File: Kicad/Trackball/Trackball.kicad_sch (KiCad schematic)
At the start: 52 parts, among them J1 Battery, J10 Conn_01x04_Female, J11 Conn_01x04_Female, J12 Conn_01x04_Female, J13 Conn_01x04_Female, J14 Conn_01x04_Female, J15 Conn_01x04_Female, J17 Conn_01x04_Female, J18 Conn_01x03_Pin, J19 Conn_01x03_Pin, J2 Conn_01x04_Male, J20 Conn_01x03_Socket, J21 Conn_01x03_Socket, J3 Conn_01x04_Male, J4 Conn_01x04_Male, J5 Conn_01x04_Male, J7 Conn_01x04_Male, J8 Conn_01x04_Male, J9 Conn_01x04_Male, SW1 SW_SPDT, SW2 SW_SPDT, SW3 SW_SPDT, U1 ProMicro, U3 TCR2EF19, U4 PMW3610

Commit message: B4: Base,  Cover, 52.5 mm ball platform ready. TODO: add 44mm platform.
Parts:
- removed H2: MountingHole_Pad, MountingHole:MountingHole_2.5mm_Pad, symbol Mechanical:MountingHole_Pad
- removed J11, J14, J17: Conn_01x04_Female, Connector_PinSocket_2.54mm:PinSocket_1x04_P2.54mm_Vertical, symbol Connector:Conn_01x04_Female
- removed J7, J8, J9: Conn_01x04_Male, Connector_PinHeader_2.54mm:PinHeader_1x04_P2.54mm_Vertical, symbol Connector:Conn_01x04_Male
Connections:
- net GND_T is gone; now on net GNDA: H3.1, H6.1, H7.1
- net Button1: now also J12.4 (Pin_4); no longer MX1.1 (COL)
- net Button2: now also MX2.2 (ROW); no longer J2.2 (Pin_2)
- net Button3: now also MX3.2 (ROW); no longer J2.3 (Pin_3)
- net Button4: now also J15.4 (Pin_4); no longer MX4.2 (ROW)
- net Button5: now also MX5.1 (COL); no longer J3.2 (Pin_2)
- net Button6: now also MX6.1 (COL); no longer J3.3 (Pin_3)
- net GND: now also J10.1 (Pin_1), J10.2 (Pin_2), J10.3 (Pin_3), J10.4 (Pin_4), J12.1 (Pin_1), J12.2 (Pin_2), J12.3 (Pin_3), J13.1 (Pin_1), J13.2 (Pin_2), J13.3 (Pin_3), J13.4 (Pin_4), J15.1 (Pin_1), J15.2 (Pin_2), J15.3 (Pin_3), MX2.1 (COL), MX3.1 (COL), MX5.2 (ROW), MX6.2 (ROW); no longer H4.1, H5.1, J4.1 (Pin_1), J4.2 (Pin_2), J4.3 (Pin_3), J4.4 (Pin_4), J5.1 (Pin_1), J5.2 (Pin_2), J5.3 (Pin_3), J5.4 (Pin_4), MX1.2 (ROW), MX4.1 (COL)
- net GNDA: now also H4.1, H5.1, J2.1 (Pin_1), J2.2 (Pin_2), J2.3 (Pin_3), J2.4 (Pin_4), J3.1 (Pin_1), J3.2 (Pin_2), J3.3 (Pin_3), J3.4 (Pin_4), J4.1 (Pin_1), J4.2 (Pin_2), J4.3 (Pin_3), MX1.2 (ROW), MX4.1 (COL); no longer J12.1 (Pin_1), J12.2 (Pin_2), J12.3 (Pin_3), J12.4 (Pin_4), J15.1 (Pin_1), J15.2 (Pin_2), J15.3 (Pin_3), J15.4 (Pin_4), MX2.1 (COL), MX3.1 (COL), MX5.2 (ROW), MX6.2 (ROW)
- new net: J4.4 (Pin_4), MX1.1 (COL)
- new net: J5.4 (Pin_4), MX4.2 (ROW)
- new net: J5.1 (Pin_1), J5.2 (Pin_2), J5.3 (Pin_3)
- no-connect marks 11 -> 2
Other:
- note removed: "Top PCB Support."
- moved on the sheet: J10, J12, J13, J15, J2, J3, J4, J5, MX1, MX4

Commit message: B4: Trying to hoax JLC to think the bottom plate is small - added pad holes instead of simple holes.
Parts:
- added H10, H11, H12, H13, H14, H15, H16, H2, H8, H9: MountingHole_Pad, MountingHole:MountingHole_3.7mm_Pad, symbol Mechanical:MountingHole_Pad
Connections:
- net GND: now also H12.1, H13.1, H14.1, H15.1, H16.1
- new net GNDB: H10.1, H11.1, H2.1, H8.1, H9.1
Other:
- note added: "Cover Plate Holes"

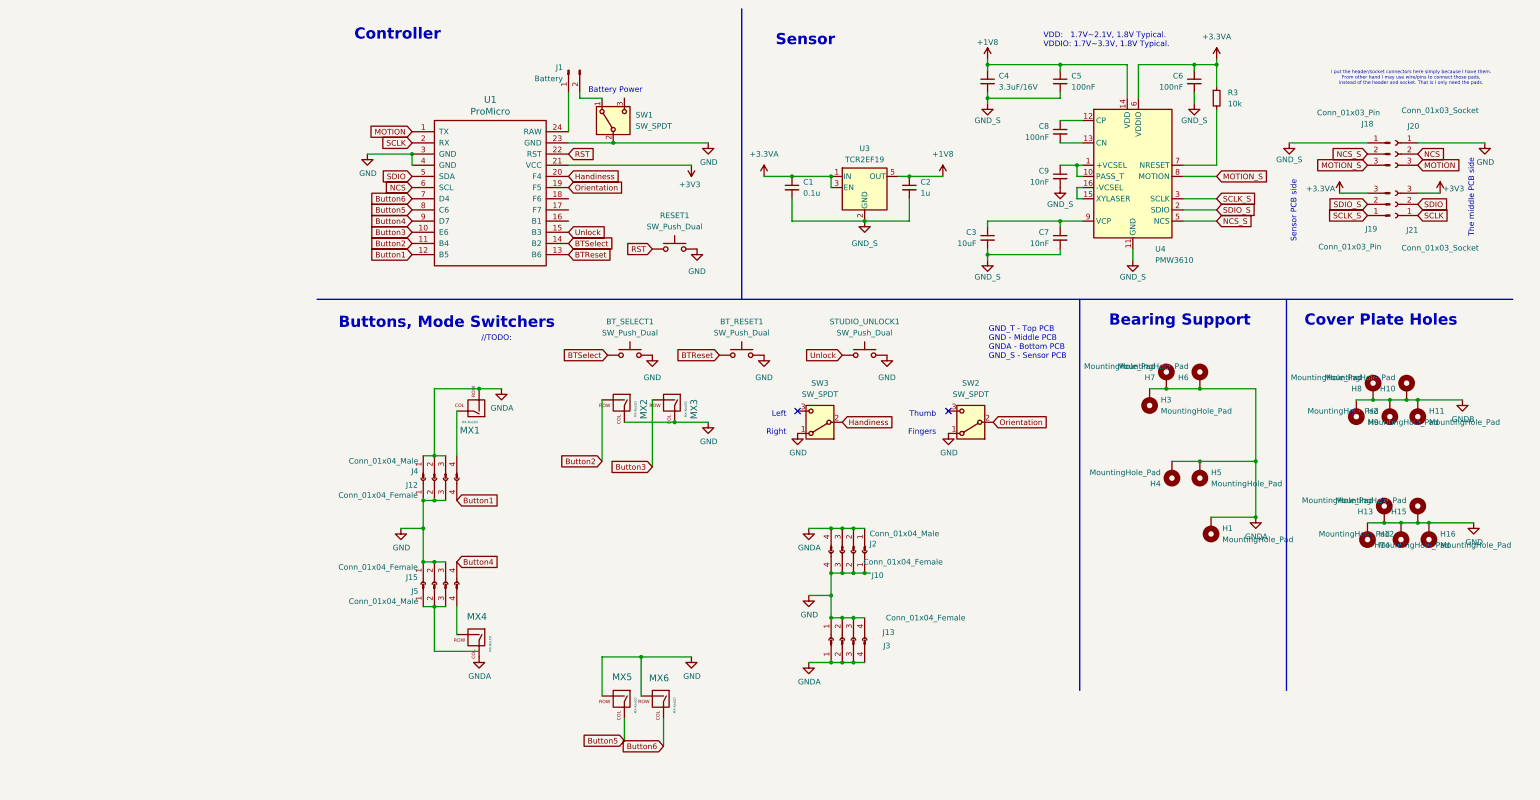
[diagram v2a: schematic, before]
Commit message: B4: Corrected the PCBs, added two more keys. TODO: add 55mm top deck.
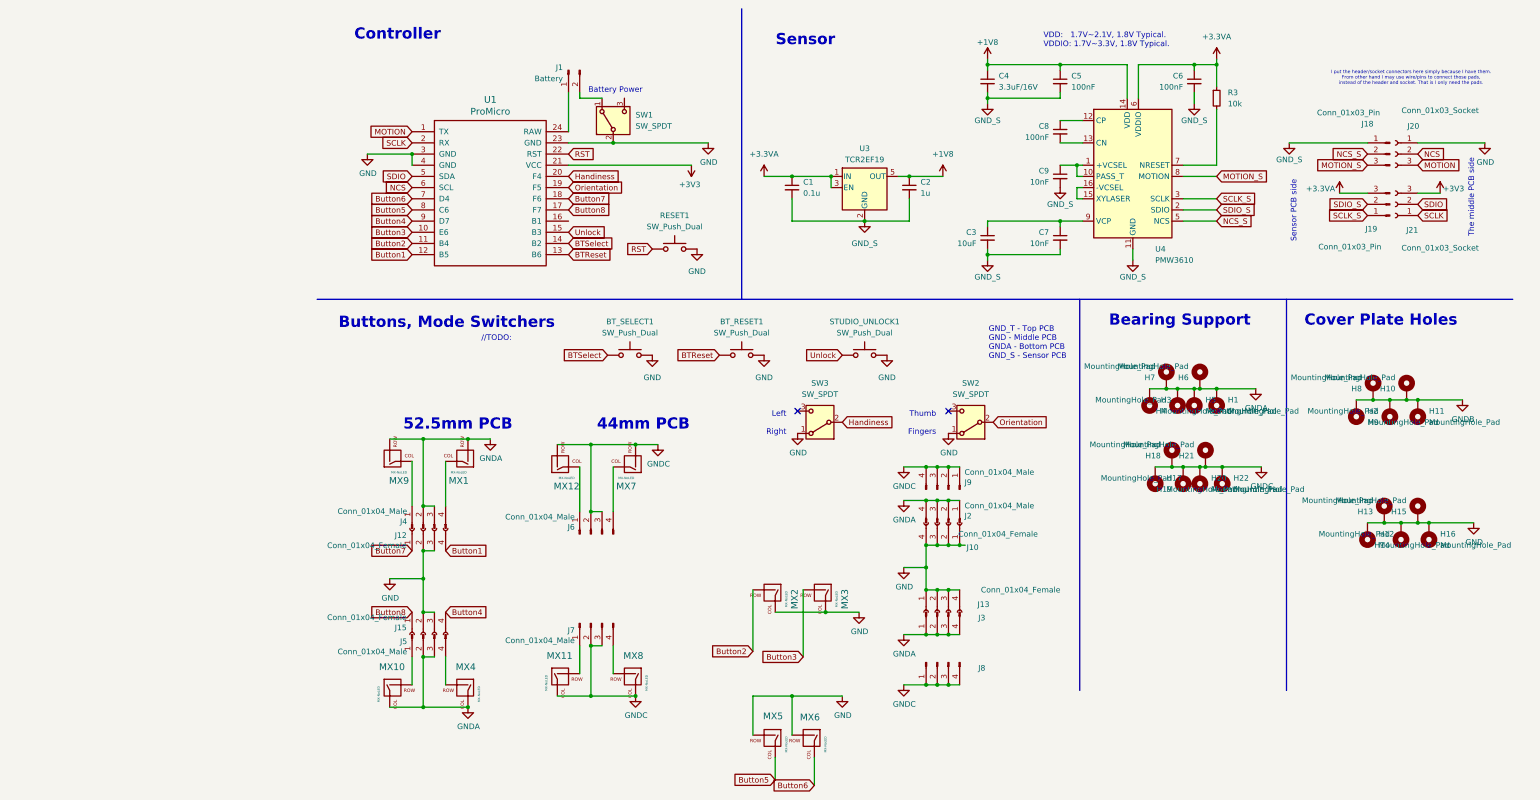
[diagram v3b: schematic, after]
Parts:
- added H17, H18, H19, H20, H21, H22: MountingHole_Pad, MountingHole:MountingHole_2.5mm_Pad, symbol Mechanical:MountingHole_Pad
- added J6, J7, J8, J9: Conn_01x04_Male, Connector_PinHeader_2.54mm:PinHeader_1x04_P2.54mm_Vertical, symbol Connector:Conn_01x04_Male
- added MX10, MX11, MX12, MX7, MX8, MX9: MX-NoLED, keyswitches.pretty-master:Kailh_socket_PG1350, symbol MX_Alps_Hybrid:MX-NoLED
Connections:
- net GND: no longer J12.1 (Pin_1), J15.1 (Pin_1)
- net GNDA: now also J5.2 (Pin_2), J5.3 (Pin_3), MX10.1 (COL), MX9.2 (ROW); no longer J4.1 (Pin_1)
- net Button8: now reaches U1.17 (F7)
- net Button8: now also J15.1 (Pin_1)
- net Button7: now reaches U1.18 (F6)
- net Button7: now also J12.1 (Pin_1)
- new net: J5.1 (Pin_1), MX10.2 (ROW)
- new net: J4.1 (Pin_1), MX9.1 (COL)
- new net: J7.4 (Pin_4), MX8.2 (ROW)
- new net: J7.1 (Pin_1), MX11.2 (ROW)
- new net: J6.1 (Pin_1), MX12.1 (COL)
- new net: J6.4 (Pin_4), MX7.1 (COL)
- new net GNDC: H17.1, H18.1, H19.1, H20.1, H21.1, H22.1, J6.2 (Pin_2), J6.3 (Pin_3), J7.2 (Pin_2), J7.3 (Pin_3), J8.1 (Pin_1), J8.2 (Pin_2), J8.3 (Pin_3), J8.4 (Pin_4), J9.1 (Pin_1), J9.2 (Pin_2), J9.3 (Pin_3), J9.4 (Pin_4), MX11.1 (COL), MX12.2 (ROW), MX7.2 (ROW), MX8.1 (COL)
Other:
- note added: "44mm PCB"
- note added: "52.5mm PCB"
- moved on the sheet: H1, H4, H5, J10, J12, J13, J15, J2, J3, J4, J5, MX1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

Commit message: B4: Added 55mm top PCB, moved the buttons  around, reduced the overall outline. TODO: lay out the wiring.
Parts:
- added H23, H24, H25, H26: MountingHole_Pad, MountingHole:MountingHole_2.5mm_Pad, symbol Mechanical:MountingHole_Pad
- added J11, J16, J17, J22, J23, J24, J25: Conn_01x04_Male, Connector_PinHeader_2.54mm:PinHeader_1x04_P2.54mm_Vertical, symbol Connector:Conn_01x04_Male
- added J14: Conn_01x04_Female, Connector_PinSocket_2.54mm:PinSocket_1x04_P2.54mm_Vertical, symbol Connector:Conn_01x04_Female
- added MX13, MX14, MX15, MX16, MX17, MX18, MX19, MX20: MX-NoLED, keyswitches.pretty-master:Kailh_socket_PG1350, symbol MX_Alps_Hybrid:MX-NoLED
- H10, H15: footprint MountingHole:MountingHole_3.7mm_Pad -> MountingHole:MountingHole_2.5mm_Pad
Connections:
- net Button3: now also J12.3 (Pin_3); no longer MX3.2 (ROW)
- net Button5: now also MX5.2 (ROW); no longer MX5.1 (COL)
- net Button6: now also J15.3 (Pin_3); no longer MX6.1 (COL)
- net GND: now also MX5.1 (COL), J14.1 (Pin_1), J14.2 (Pin_2), J14.3 (Pin_3), J14.4 (Pin_4); no longer H15.1, J12.3 (Pin_3), J15.3 (Pin_3), MX3.1 (COL), MX5.2 (ROW), MX6.2 (ROW)
- net GNDA: now also MX3.2 (ROW), MX6.1 (COL), J16.1 (Pin_1), J16.2 (Pin_2), J16.3 (Pin_3), J16.4 (Pin_4); no longer J4.3 (Pin_3), J5.3 (Pin_3)
- net GNDB: no longer H10.1
- net GNDC: now also J11.1 (Pin_1), J11.2 (Pin_2), J11.3 (Pin_3), J11.4 (Pin_4), MX13.1 (COL), MX14.2 (ROW); no longer J6.3 (Pin_3), J7.3 (Pin_3)
- new net: J4.3 (Pin_3), MX3.1 (COL)
- new net: J5.3 (Pin_3), MX6.2 (ROW)
- new net: J23.1 (Pin_1), MX16.2 (ROW)
- new net: J23.3 (Pin_3), MX18.2 (ROW)
- new net: J23.4 (Pin_4), MX20.2 (ROW)
- new net: J22.3 (Pin_3), MX17.1 (COL)
- new net: J7.3 (Pin_3), MX13.2 (ROW)
- new net: J22.4 (Pin_4), MX19.1 (COL)
- new net: J6.3 (Pin_3), MX14.1 (COL)
- new net: J22.1 (Pin_1), MX15.1 (COL)
- new net GNDE: H10.1, H15.1, H23.1, H24.1, H25.1, H26.1, J17.1 (Pin_1), J17.2 (Pin_2), J17.3 (Pin_3), J17.4 (Pin_4), J22.2 (Pin_2), J23.2 (Pin_2), J24.1 (Pin_1), J24.2 (Pin_2), J24.3 (Pin_3), J24.4 (Pin_4), J25.1 (Pin_1), J25.2 (Pin_2), J25.3 (Pin_3), J25.4 (Pin_4), MX15.2 (ROW), MX16.1 (COL), MX17.2 (ROW), MX18.1 (COL), MX19.2 (ROW), MX20.1 (COL)
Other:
- note added: "55mm PCB"
- note added: "GND - Middle PCB GNDA - 52.5mm Top PCB GNDB - Bottom Cover GNDC - 44mm Top PCB GNDE - 55 mm Top PCb GND_S - Sensor PCB"
- note removed: "GND_T - Top PCB GND - Middle PCB GNDA - Bottom PCB GND_S - Sensor PCB"
- moved on the sheet: J10, J13, J2, J3, J6, J7, J8, J9, MX1, MX11, MX12, MX2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

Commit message: B4: Flipped n!n to the back side, facing up - to the  board.
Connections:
- net GND: now also SW3.3 (C); no longer SW3.1 (A)
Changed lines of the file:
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@@
 	(text "44mm PCB"
 		(exclude_from_sim no)
-		(at 109.728 105.918 0)
+		(at 87.122 105.664 0)
 		(effects
 			(font
@@
 	)
 	(no_connect
-		(at 121.92 102.87)
+		(at 121.92 107.95)
 	)
 	(wire
@@
 	(symbol
 		(lib_id "power:GND")
-		(at 121.92 107.95 0)
+		(at 121.92 102.87 0)
 		(unit 1)
 		(exclude_from_sim no)
@@
 		(dnp no)
 		(property "Reference" "#PWR028"
-			(at 121.92 114.3 0)
+			(at 121.92 109.22 0)
 			(effects
 				(font
@@
 		)
 		(property "Value" "GND"
-			(at 122.047 112.3442 0)
+			(at 120.142 101.854 0)
 			(effects
 				(font
@@
 		)
 		(property "Footprint" ""
-			(at 121.92 107.95 0)
+			(at 121.92 102.87 0)
 			(effects
 				(font
@@
 		)
 		(property "Datasheet" ""
-			(at 121.92 107.95 0)
+			(at 121.92 102.87 0)
 			(effects
 				(font
@@
 		)
 		(property "Description" ""
-			(at 121.92 107.95 0)
+			(at 121.92 102.87 0)
 			(effects
 				(font
